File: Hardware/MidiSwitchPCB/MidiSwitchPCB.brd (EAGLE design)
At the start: 160 x 100 mm, 77 parts, among them IC3 74LVC2G04GW,125, J1 694108106102, Q1 BSS123, Q2 BSS123, Q3 BSS123, Q4 BSS123, Q5 BSS123, Q6 BSS123, Q7 BSS123, Q8 BSS123, X1 1503_09, X2 1503_09, X3 1503_09, X4 1503_09

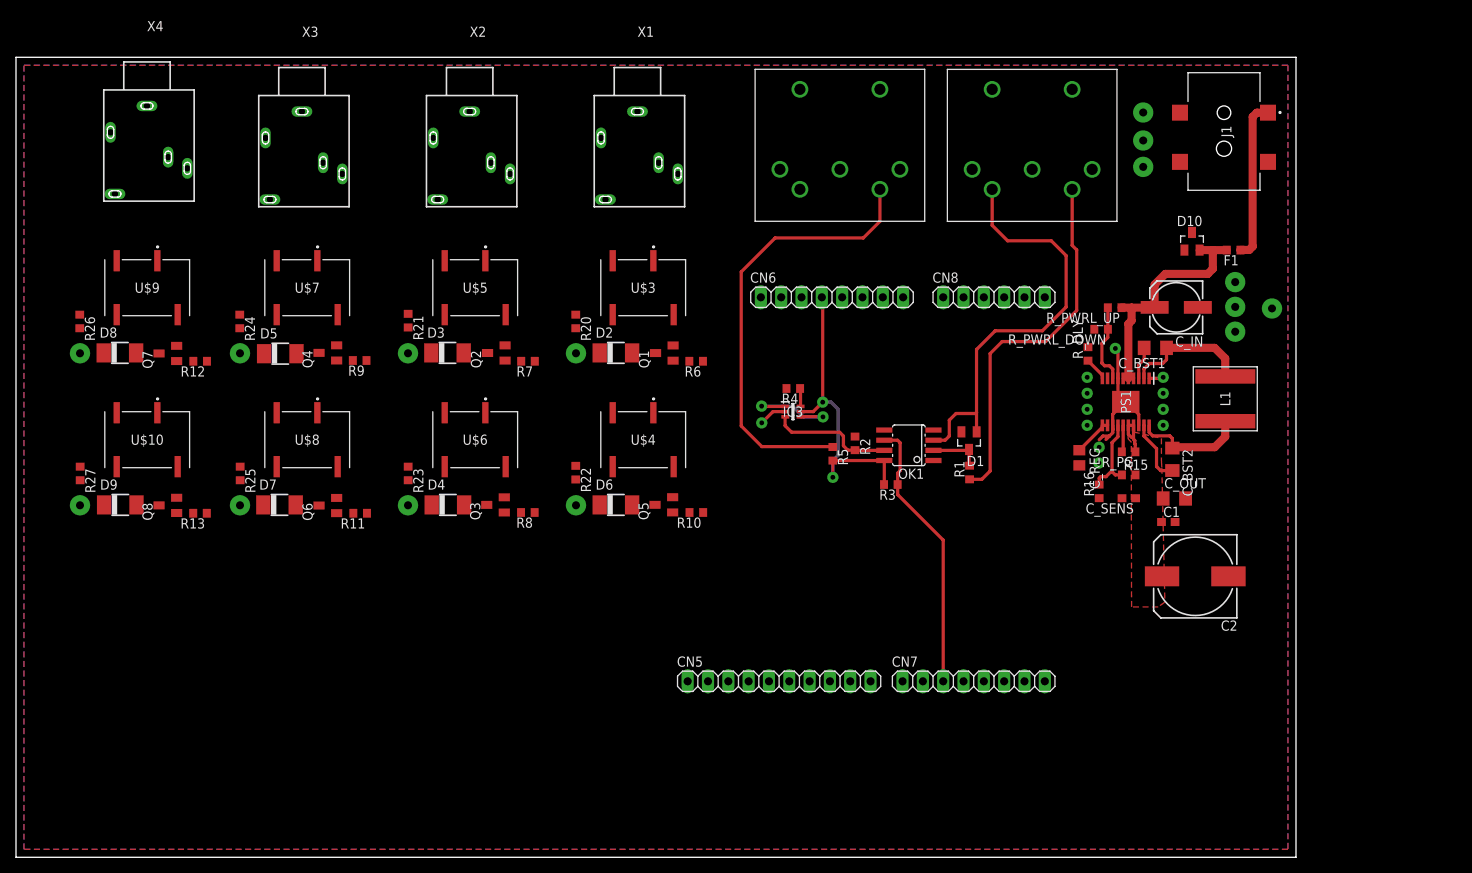
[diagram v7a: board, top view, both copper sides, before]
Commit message: continued layout design. The pinheaders are unfortunately connected on the wrong pcb side.
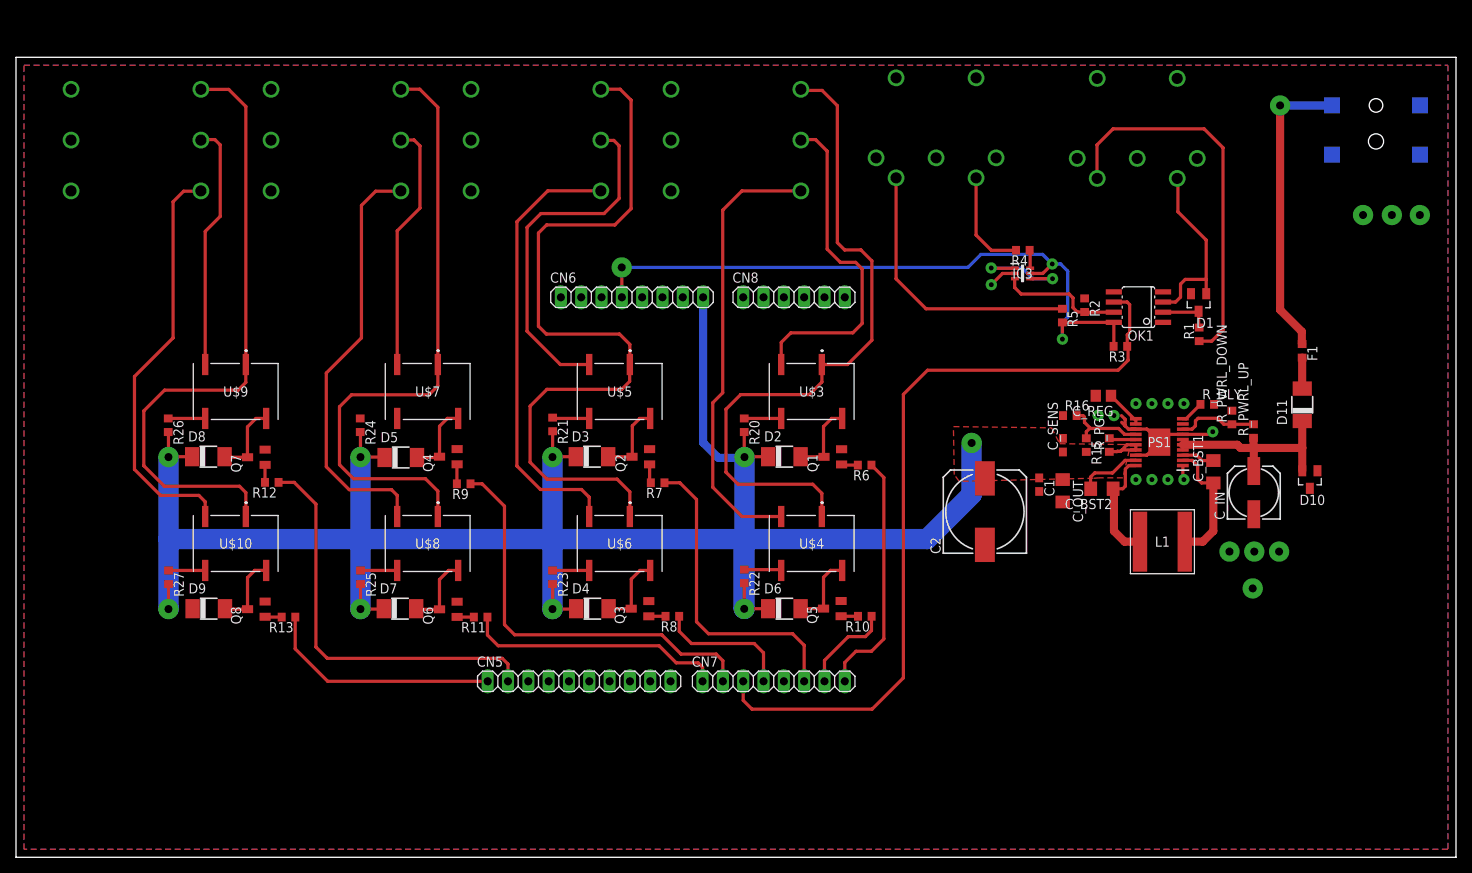
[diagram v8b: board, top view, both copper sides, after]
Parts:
- removed X1, X2, X3, X4: 1503_09, con-lumberg:1503_09
- added D11: (no value), diode:DO-214AC
- added J2, J3, J4, J5: NMJ6HCD2, NMJ6HCD2:NMJ6HCD2
- moved D1 33.5 mm to (147.8, 69.4)
- moved R5 33.5 mm to (130.8, 67.7)
- moved OK1 33.5 mm to (140.3, 68.8)
- moved R2 33.5 mm to (133.6, 69.0)
- moved R3 33.5 mm to (138.0, 63.9)
- moved IC3 33.5 mm to (125.8, 73.0)
- moved R1 33.5 mm to (147.9, 65.4)
- moved R4 33.5 mm to (125.9, 75.9)
- moved D10 33.2 mm to (161.7, 47.2), turned to 180 degrees
- moved C2 27.5 mm to (121.1, 43.2), turned to 90 degrees
- moved C_IN 25.1 mm to (154.7, 45.6), turned to 90 degrees
- moved CN5 25.0 mm to (70.4, 22.0)
- moved CN6 25.0 mm to (77.0, 70.0)
- moved CN7 25.0 mm to (94.7, 22.0)
- moved CN8 25.0 mm to (97.2, 70.0)
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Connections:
- net N$28 renamed CN7-2
- removed net N$18: CN7.4, R7.1
- removed net N$31: CN7.6, R6.1
- removed net N$40: CN7.1, R12.1
- removed net N$42: U$10.4, X4.2
- removed net N$44: CN7.8, R13.1
- removed net N$45: CN5.2, R8.1
- removed net N$46: CN7.7, R11.1
- removed net N$47: CN5.1, R10.1
- new net CN5-1: CN5.1, R13.1
- new net CN5-2: CN5.2, R12.1
- new net CN7-1: CN7.1, R11.1
- new net CN7-4: CN7.4, R8.1
- new net CN7-6: CN7.6, R7.1
- new net CN7-7: CN7.7, R10.1
- new net CN7-8: CN7.8, R6.1
- new net N$50: J5.6, U$10.4
- new net N$66: D11.A, F1.2
- net GND: now also J2.1, J2.2, J2.3, J3.1, J3.2, J3.3, J4.1, J4.2, J4.3, J5.1, J5.2, J5.3
- net N$19: now also J3.5; no longer X2.5
- net N$22: now also J3.6; no longer X2.2
- net N$23: now also J3.4; no longer X2.1
- net N$29: now also J4.6, U$8.4; no longer U$7.4, X3.5
- net N$30: now also J4.5, U$7.4; no longer U$8.4, X3.2
- net N$32: now also J4.4; no longer X3.1
- net N$36: now also J2.5; no longer X1.5
- net N$37: now also J2.6; no longer X1.2
- net N$38: now also J2.4; no longer X1.1
- net N$41: now also J5.5; no longer X4.5
- net N$43: now also J5.4; no longer X4.1
- net VIN_FUSED: now also D11.C; no longer F1.2
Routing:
- net VCC_6-8: track 5.74 -> 270.1 mm, vias 8 -> 10
- net N$23: track 0.00 -> 97.2 mm
- net N$38: track 0.00 -> 84.6 mm
- net N$43: track 0.00 -> 79.2 mm
- net N$32: track 0.00 -> 77.8 mm
- net N$9: track 34.4 -> 99.0 mm
- net N$37: track 0.00 -> 56.0 mm
- net N$22: track 0.00 -> 55.7 mm
- net N$29: track 0.00 -> 53.2 mm
- net CN7-2: track 0.00 -> 52.0 mm
- net N$50: track 0.00 -> 51.9 mm
- net CN5-2: track 0.00 -> 50.7 mm
- net VCC_3_3: track 39.0 -> 84.6 mm, vias 2 -> 3
- net N$19: track 0.00 -> 44.6 mm
- net N$36: track 0.00 -> 42.2 mm
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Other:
- board size 160 x 100 mm -> 180 x 100 mm
